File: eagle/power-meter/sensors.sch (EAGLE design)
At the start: 36 parts

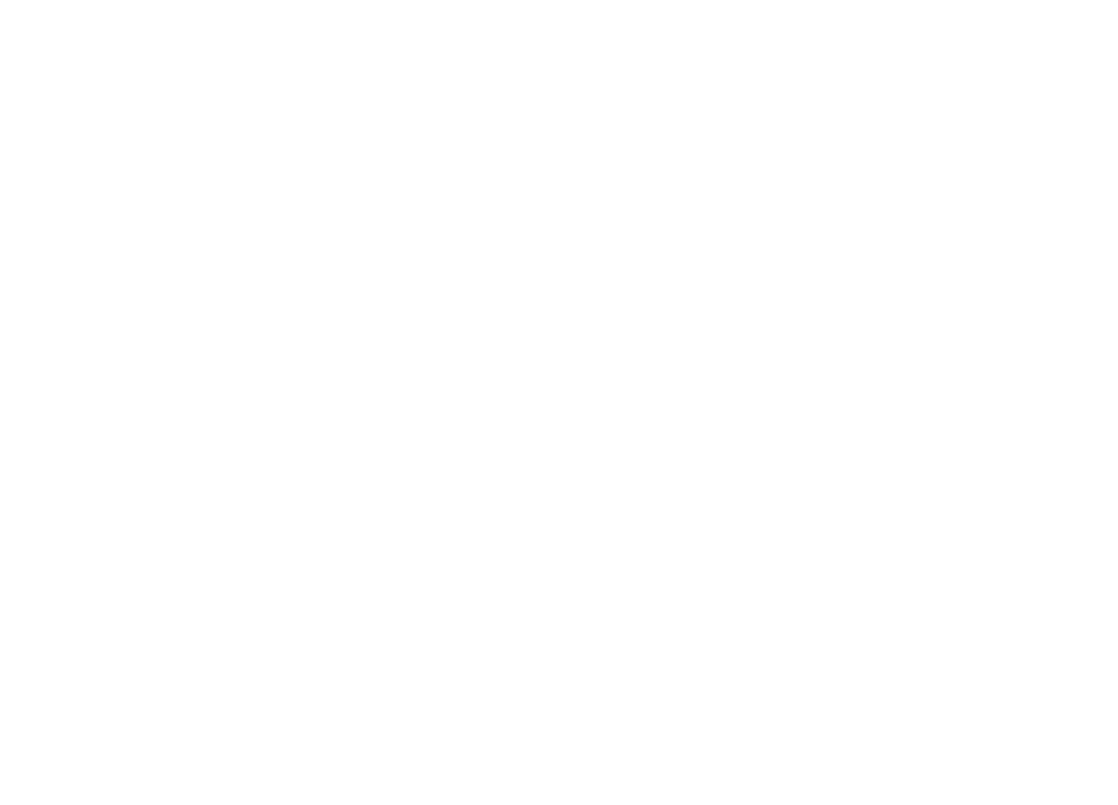
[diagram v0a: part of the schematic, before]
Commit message: Common Eagle library created. Working on power-node schematics
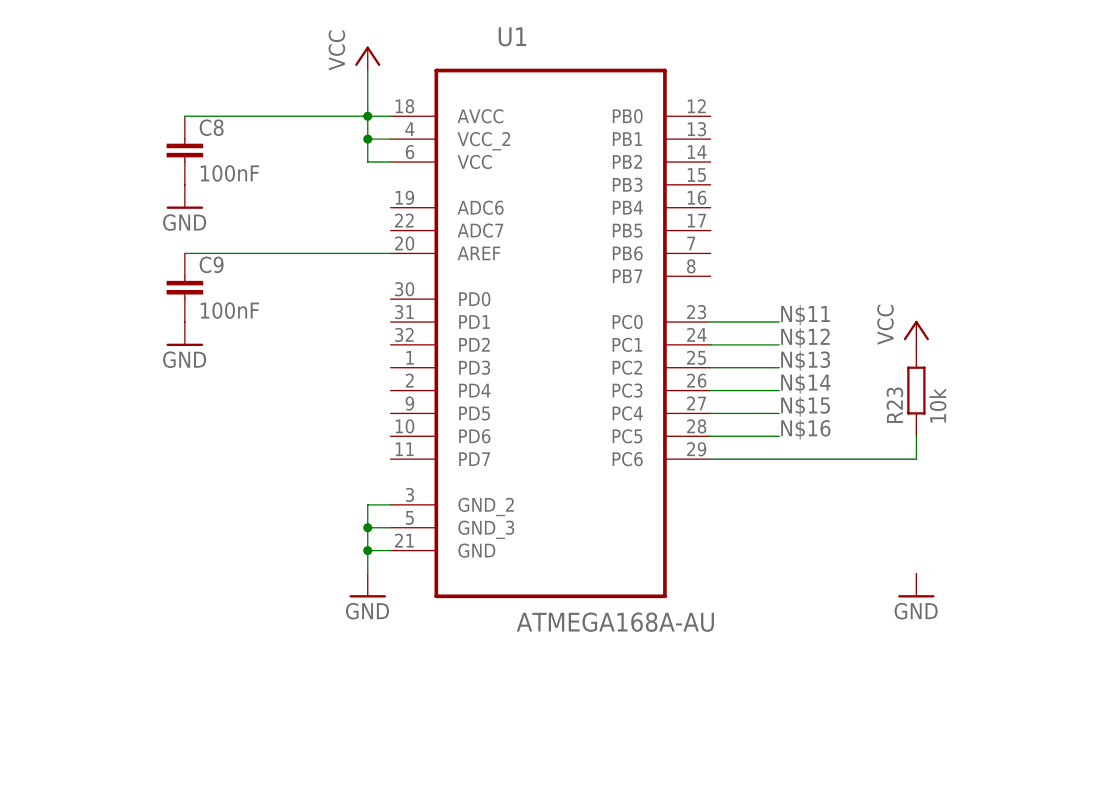
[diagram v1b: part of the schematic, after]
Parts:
- added C8, C9: 100nF, rcl:C-EUC1206
- added R23: 10k, rcl:R-EU_R1206
- added U1: ATMEGA168A-AU, Atmel_By_element14_Batch_1:ATMEGA168A-AU
- JC1: device Jack3.5:15428/BT -> EnergyMonitoring:15428/BT
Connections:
- new net N$10: R23.1, U1.PC6
- new net N$11: U1.PC0
- new net N$12: U1.PC1
- new net N$13: U1.PC2
- new net N$14: U1.PC3
- new net N$15: U1.PC4
- new net N$16: U1.PC5
- new net N$9: C9.1, U1.AREF
- net GND: now also C8.2, C9.2, U1.GND, U1.GND_2, U1.GND_3
- net VCC: now also C8.1, R23.2, U1.AVCC, U1.VCC, U1.VCC_2
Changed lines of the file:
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@@
 <part name="C2" library="rcl" deviceset="CPOL-EU" device="153CLV-0405" value="10uF"/>
 <part name="GND1" library="supply1" deviceset="GND" device=""/>
-<part name="JC1" library="Jack3.5" deviceset="15428/BT" device=""/>
+<part name="JC1" library="EnergyMonitoring" deviceset="15428/BT" device=""/>
 <part name="R8" library="rcl" deviceset="R-EU_" device="R1206" value="120"/>
 <part name="R9" library="rcl" deviceset="R-EU_" device="R1206" value="470k"/>
@@
 <part name="GND7" library="supply1" deviceset="GND" device=""/>
 <part name="JC6" library="Jack3.5" deviceset="15428/BT" device=""/>
+<part name="U1" library="Atmel_By_element14_Batch_1" deviceset="ATMEGA168A-AU" device=""/>
+<part name="P+8" library="supply1" deviceset="VCC" device=""/>
+<part name="GND8" library="supply1" deviceset="GND" device=""/>
+<part name="C8" library="rcl" deviceset="C-EU" device="C1206" value="100nF"/>
+<part name="GND9" library="supply1" deviceset="GND" device=""/>
+<part name="C9" library="rcl" deviceset="C-EU" device="C1206" value="100nF"/>
+<part name="GND10" library="supply1" deviceset="GND" device=""/>
+<part name="R23" library="rcl" deviceset="R-EU_" device="R1206" value="10k"/>
+<part name="P+9" library="supply1" deviceset="VCC" device=""/>
+<part name="GND11" library="supply1" deviceset="GND" device=""/>
 </parts>
 <sheets>
@@
 <instance part="GND7" gate="1" x="137.16" y="7.62"/>
 <instance part="JC6" gate="J$1" x="116.84" y="33.02"/>
+<instance part="U1" gate="A" x="129.54" y="144.78"/>
+<instance part="P+8" gate="VCC" x="109.22" y="172.72"/>
+<instance part="GND8" gate="1" x="109.22" y="111.76"/>
+<instance part="C8" gate="G$1" x="88.9" y="162.56"/>
+<instance part="GND9" gate="1" x="88.9" y="154.94"/>
+<instance part="C9" gate="G$1" x="88.9" y="147.32"/>
+<instance part="GND10" gate="1" x="88.9" y="139.7"/>
+<instance part="R23" gate="G$1" x="170.18" y="134.62" rot="R90"/>
+<instance part="P+9" gate="VCC" x="170.18" y="142.24"/>
+<instance part="GND11" gate="1" x="170.18" y="111.76"/>
 </instances>
 <busses>
@@
 <junction x="137.16" y="10.16"/>
 </segment>
+<segment>
+<pinref part="GND8" gate="1" pin="GND"/>
+<pinref part="U1" gate="A" pin="GND"/>
+<wire x1="109.22" y1="114.3" x2="109.22" y2="116.84" width="0.1524" layer="91"/>
+<wire x1="109.22" y1="116.84" x2="111.76" y2="116.84" width="0.1524" layer="91"/>
+<pinref part="U1" gate="A" pin="GND_3"/>
+<wire x1="109.22" y1="116.84" x2="109.22" y2="119.38" width="0.1524" layer="91"/>
+<wire x1="109.22" y1="119.38" x2="111.76" y2="119.38" width="0.1524" layer="91"/>
+<junction x="109.22" y="116.84"/>
+<pinref part="U1" gate="A" pin="GND_2"/>
+<wire x1="109.22" y1="119.38" x2="109.22" y2="121.92" width="0.1524" layer="91"/>
+<wire x1="109.22" y1="121.92" x2="111.76" y2="121.92" width="0.1524" layer="91"/>
+<junction x="109.22" y="119.38"/>
+</segment>
+<segment>
+<pinref part="C8" gate="G$1" pin="2"/>
+<pinref part="GND9" gate="1" pin="GND"/>
+</segment>
+<segment>
+<pinref part="C9" gate="G$1" pin="2"/>
+<pinref part="GND10" gate="1" pin="GND"/>
+</segment>
 </net>
 <net name="VCC" class="0">
@@
 <pinref part="R21" gate="G$1" pin="2"/>
 <pinref part="P+7" gate="VCC" pin="VCC"/>
+</segment>
+<segment>
+<pinref part="P+8" gate="VCC" pin="VCC"/>
+<pinref part="U1" gate="A" pin="AVCC"/>
+<wire x1="109.22" y1="170.18" x2="109.22" y2="165.1" width="0.1524" layer="91"/>
+<wire x1="109.22" y1="165.1" x2="111.76" y2="165.1" width="0.1524" layer="91"/>
+<pinref part="U1" gate="A" pin="VCC_2"/>
+<wire x1="109.22" y1="162.56" x2="111.76" y2="162.56" width="0.1524" layer="91"/>
+<junction x="109.22" y="165.1"/>
+<pinref part="U1" gate="A" pin="VCC"/>
+<wire x1="109.22" y1="162.56" x2="109.22" y2="160.02" width="0.1524" layer="91"/>
+<wire x1="109.22" y1="160.02" x2="111.76" y2="160.02" width="0.1524" layer="91"/>
+<junction x="109.22" y="162.56"/>
+<pinref part="C8" gate="G$1" pin="1"/>
+<wire x1="109.22" y1="162.56" x2="109.22" y2="165.1" width="0.1524" layer="91"/>
+<wire x1="109.22" y1="165.1" x2="88.9" y2="165.1" width="0.1524" layer="91"/>
+</segment>
+<segment>
+<pinref part="R23" gate="G$1" pin="2"/>
+<pinref part="P+9" gate="VCC" pin="VCC"/>
 </segment>
 </net>
@@
 </segment>
 </net>
+<net name="N$9" class="0">
+<segment>
+<pinref part="U1" gate="A" pin="AREF"/>
+<pinref part="C9" gate="G$1" pin="1"/>
+<wire x1="111.76" y1="149.86" x2="88.9" y2="149.86" width="0.1524" layer="91"/>
+</segment>
+</net>
+<net name="N$10" class="0">
+<segment>
+<pinref part="U1" gate="A" pin="PC6"/>
+<wire x1="147.32" y1="127" x2="170.18" y2="127" width="0.1524" layer="91"/>
+<pinref part="R23" gate="G$1" pin="1"/>
+<wire x1="170.18" y1="127" x2="170.18" y2="129.54" width="0.1524" layer="91"/>
+</segment>
+</net>
+<net name="N$11" class="0">
+<segment>
+<pinref part="U1" gate="A" pin="PC0"/>
+<wire x1="147.32" y1="142.24" x2="154.94" y2="142.24" width="0.1524" layer="91"/>
+<label x="154.94" y="142.24" size="1.778" layer="95"/>
+</segment>
+</net>
+<net name="N$12" class="0">
+<segment>
+<pinref part="U1" gate="A" pin="PC1"/>
+<wire x1="147.32" y1="139.7" x2="154.94" y2="139.7" width="0.1524" layer="91"/>
+<label x="154.94" y="139.7" size="1.778" layer="95"/>
+</segment>
+</net>
+<net name="N$13" class="0">
+<segment>
+<pinref part="U1" gate="A" pin="PC2"/>
+<wire x1="147.32" y1="137.16" x2="154.94" y2="137.16" width="0.1524" layer="91"/>
+<label x="154.94" y="137.16" size="1.778" layer="95"/>
+</segment>
+</net>
+<net name="N$14" class="0">
+<segment>
+<pinref part="U1" gate="A" pin="PC3"/>
+<wire x1="147.32" y1="134.62" x2="154.94" y2="134.62" width="0.1524" layer="91"/>
+<label x="154.94" y="134.62" size="1.778" layer="95"/>
+</segment>
+</net>
+<net name="N$15" class="0">
+<segment>
+<pinref part="U1" gate="A" pin="PC4"/>
+<wire x1="147.32" y1="132.08" x2="154.94" y2="132.08" width="0.1524" layer="91"/>
+<label x="154.94" y="132.08" size="1.778" layer="95"/>
+</segment>
+</net>
+<net name="N$16" class="0">
+<segment>
+<pinref part="U1" gate="A" pin="PC5"/>
+<wire x1="147.32" y1="129.54" x2="154.94" y2="129.54" width="0.1524" layer="91"/>
+<label x="154.94" y="129.54" size="1.778" layer="95"/>
+</segment>
+</net>

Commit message: Working on power-monitor PCB
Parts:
- added U$1: EVQQ2, EnergyMonitoring:EVQQ2
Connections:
- net N$9 renamed AREF
- removed net N$12: U1.PC1
- removed net N$13: U1.PC2
- removed net N$14: U1.PC3
- removed net N$15: U1.PC4
- removed net N$16: U1.PC5
- new net RESET: R23.1, U$1.1, U$1.2, U1.PC6
- net CT1: now also U1.ADC7
- net CT2: now also U1.PC0
- net CT3: now also U1.PC1
- net CT4: now also U1.PC2
- net CT5: now also U1.PC3
- net CT6: now also U1.PC4
- net GND: now also U$1.3, U$1.4
- net N$10: now also U1.PB6; no longer R23.1, U1.PC6
- net N$11: now also U1.PB7; no longer U1.PC0
- net VT: now also U1.PC5
